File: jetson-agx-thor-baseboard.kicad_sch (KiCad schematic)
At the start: 4 parts

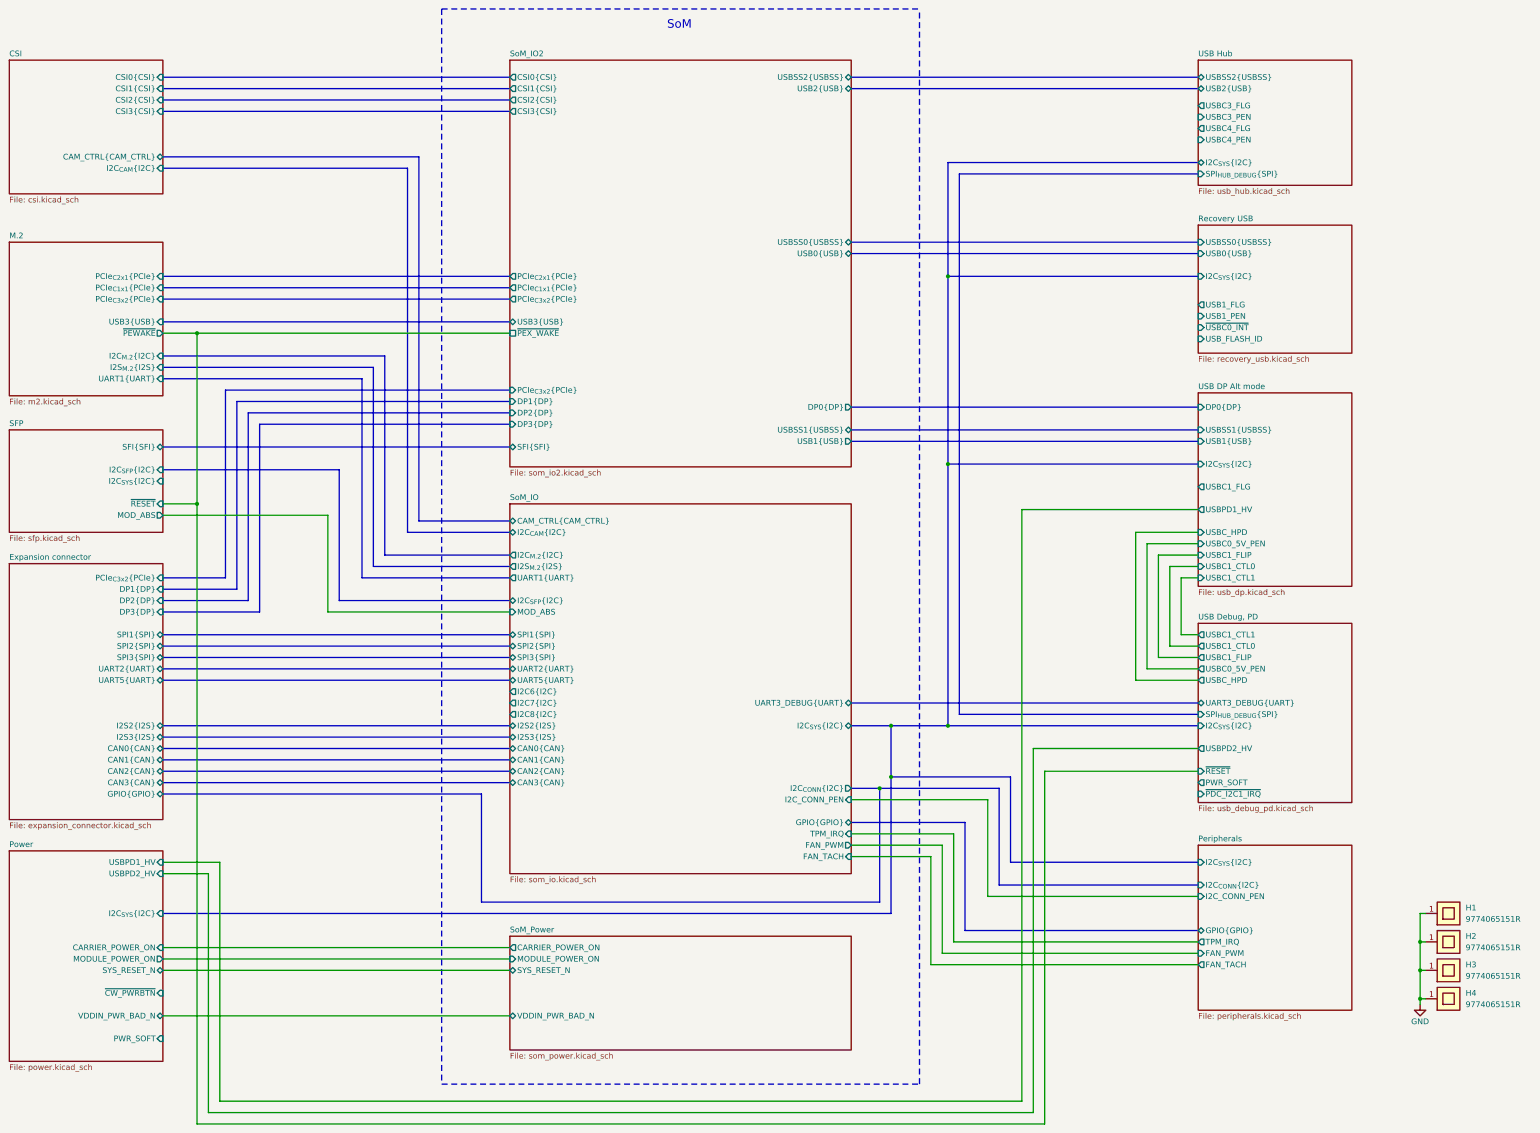
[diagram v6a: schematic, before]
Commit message: [#82837] Finish mapping interfaces, waiting for new SoM symbol
[#82837] Add GPIO level shifter and route USB related GPIO on root
schematic

[#82837] WIP: Modify Power-up and reset section
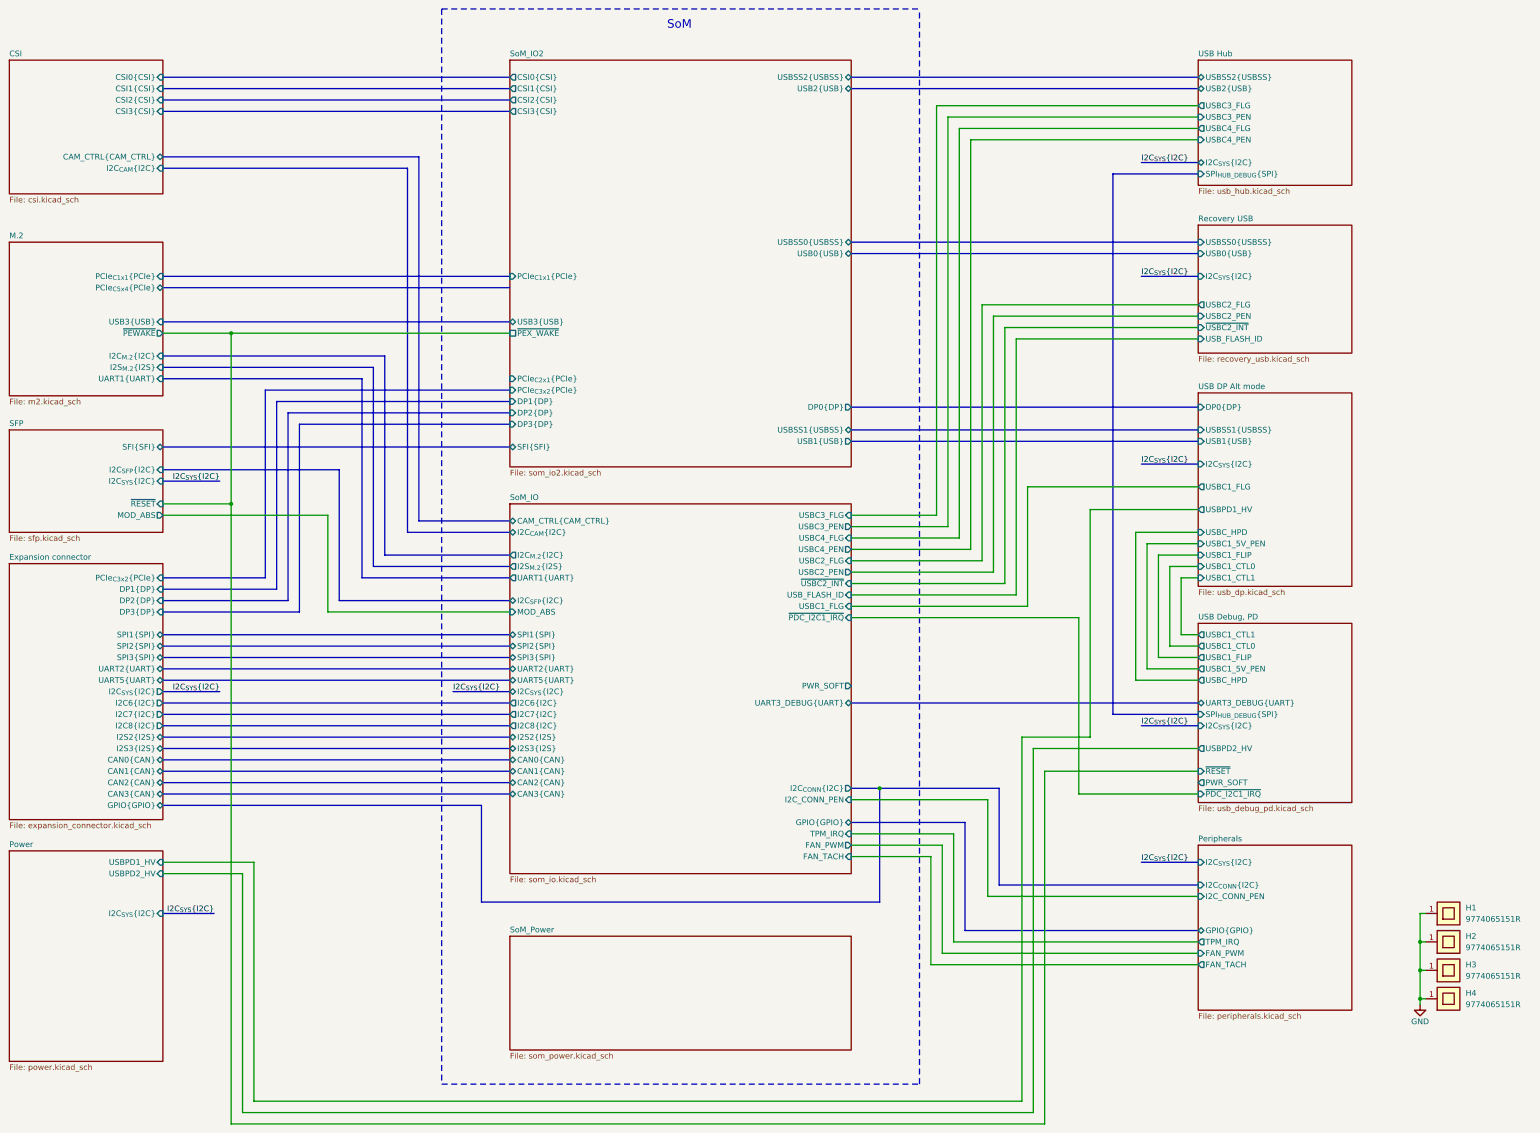
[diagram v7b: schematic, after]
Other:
- sheet Expansion connector ports: added I2C6{I2C}, I2C7{I2C}, I2C8{I2C}, I2C_{SYS}{I2C}; removed none
- sheet M.2 ports: added PCIe_{C5x4}{PCIe}; removed PCIe_{C2x1}{PCIe}, PCIe_{C3x2}{PCIe}
- sheet Power ports: added none; removed CARRIER_POWER_ON, MODULE_POWER_ON, PWR_SOFT, SYS_RESET_N, VDDIN_PWR_BAD_N, ~{CW_PWRBTN}
- sheet Recovery USB ports: added USBC2_FLG, USBC2_PEN, ~{USBC2_INT}; removed USB1_FLG, USB1_PEN, ~{USBC0_INT}
- sheet SoM_IO ports: added PWR_SOFT, USBC1_FLG, USBC2_FLG, USBC2_PEN, USBC3_FLG, USBC3_PEN, USBC4_FLG, USBC4_PEN, USB_FLASH_ID, ~{PDC_I2C1_IRQ}, ~{USBC2_INT}; removed none
- sheet SoM_Power ports: added none; removed CARRIER_POWER_ON, MODULE_POWER_ON, SYS_RESET_N, VDDIN_PWR_BAD_N
- sheet USB DP Alt mode ports: added USBC1_5V_PEN; removed USBC0_5V_PEN
- sheet USB Debug, PD ports: added USBC1_5V_PEN; removed USBC0_5V_PEN

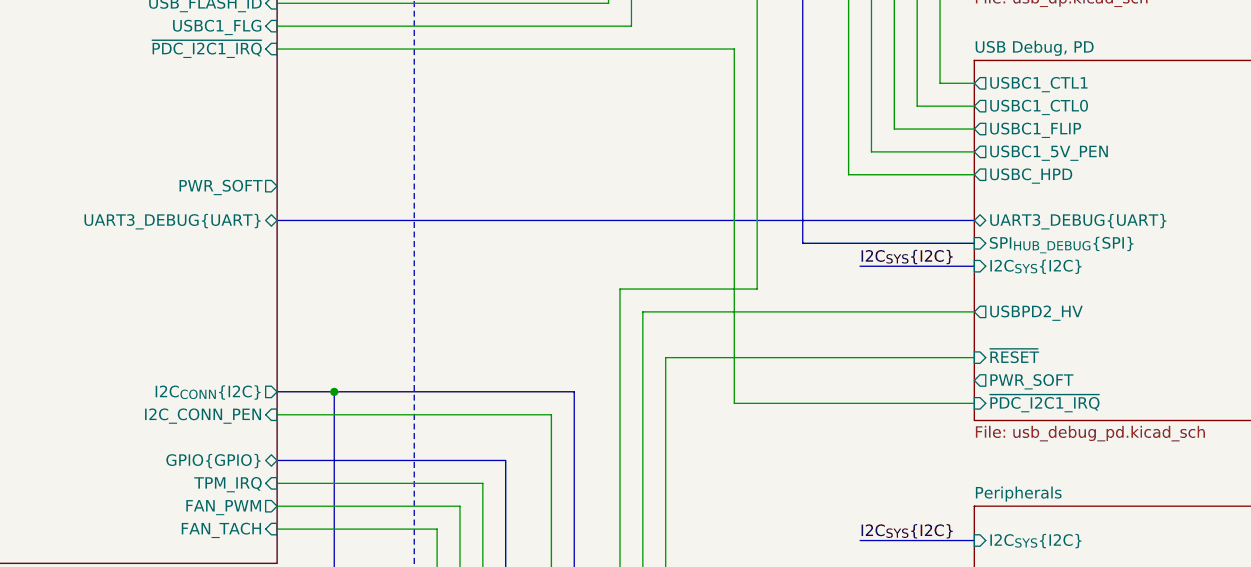
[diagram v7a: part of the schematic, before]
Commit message: [#82837] Assign leftover GPIO pins its place on SoM
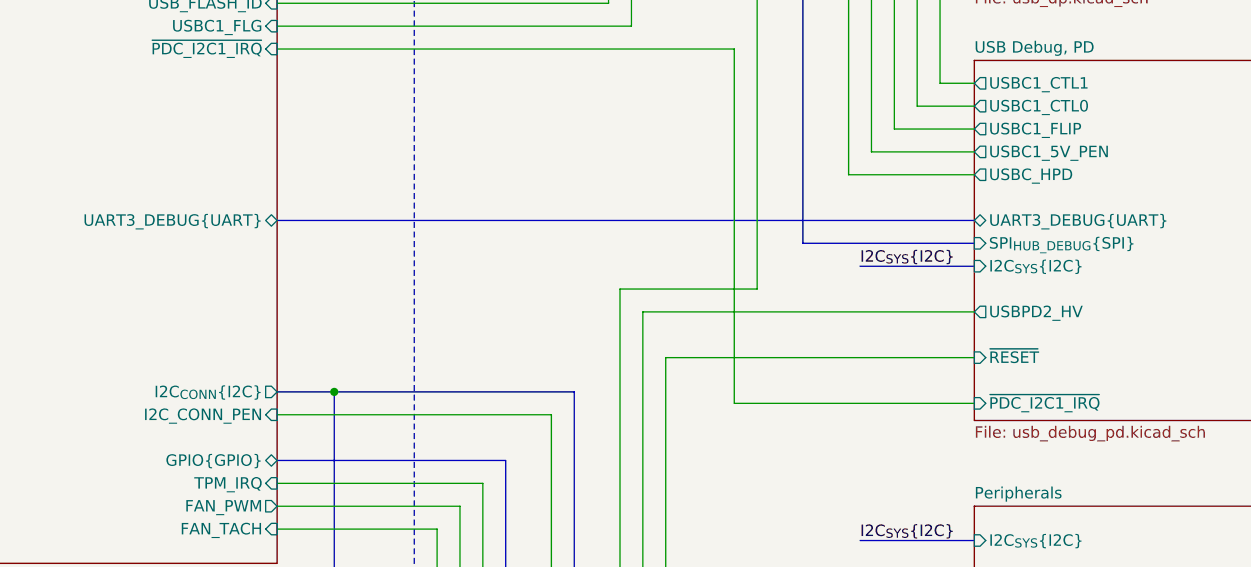
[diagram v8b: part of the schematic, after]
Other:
- sheet SoM_IO ports: added none; removed PWR_SOFT
- sheet USB Debug, PD ports: added none; removed PWR_SOFT
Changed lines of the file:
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@@
-			)
-		)
-		(pin "PWR_SOFT" output
-			(at 331.47 194.31 180)
-			(effects
-				(font
-					(size 1.27 1.27)
-				)
-				(justify left)
 			)
 		)
@@
 			)
 		)
-		(pin "PWR_SOFT" output
-			(at 254 172.72 0)
-			(effects
-				(font
-					(size 1.27 1.27)
-				)
-				(justify right)
-			)
-		)
